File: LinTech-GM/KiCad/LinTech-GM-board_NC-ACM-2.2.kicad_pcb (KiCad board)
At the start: 2 copper layers, 168.9 x 106.7 mm, 78 parts, among them Q1 12000 KHz, X1 Conn_01x08_Male, X2 Conn_01x08_Male, X3 Conn_01x08_Male, X4 Conn_01x08_Male, X7 Conn_02x03_Counter_Clockwise

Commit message: Initial 2
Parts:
- R1: value R1 -> 3.3K
- R11: value R11 -> K10
- R12: value R12 -> 3.3K
- R13, R3: value R -> 470
- R14: value R14 -> 47K
- R2, R4: value R -> 1K
- R5: value R5 -> 150
- R6: value R6 -> 91R
- R7: value R7 -> 91R
- R9: value R9 -> 470 ??
- VD1: value VD1 -> КД522Б
- VD2: value VD2 -> КД522Б
- VD3: value VD3 -> КД522Б
- VD4: value ~ -> КД522Б
- VT1, VT4: value КТ315Б -> КТ646Б
- VT5: value КТ315Б -> КТ313Б ?
- moved VD3 12.7 mm to (203.2, 70.5), turned to 0 degrees
- moved VD4 12.7 mm to (205.7, 114.9), turned to 180 degrees
- moved VD1 12.7 mm to (80.0, 36.2), turned to 270 degrees
- moved VD2 12.7 mm to (63.5, 32.4), turned to 0 degrees
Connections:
- DD3 pad 7: Net-(DD3-Pad7) -> DD5-OE
- R9 pad 1: Net-(R9-Pad1) -> Net-(R10-Pad1)
- VD1 pad 1: /DD10_Out11 -> +5V
- VD1 pad 2: +5V -> /DD10_Out11
- VD2 pad 1: Net-(DD10-Pad1) -> +5V
- VD2 pad 2: +5V -> Net-(DD10-Pad1)
- VD3 pad 1: Net-(C3-Pad1) -> +5V
- VD3 pad 2: +5V -> Net-(C3-Pad1)
- VD4 pad 1: +5V -> Net-(R14-Pad2)
- VD4 pad 2: Net-(R14-Pad2) -> +5V
- VT3 pad 2: Net-(VT3-Pad2) -> +5V
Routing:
- net DD5-OE: track 163.7 -> 178.5 mm
- net +5V: track 855.5 -> 860.5 mm
- net Net-(R10-Pad1): track 2.54 -> 5.08 mm
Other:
- board text added: "Reconstruction by Gryphon@Night-Gryphon.ru"

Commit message: BOM
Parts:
- C12: value C12 -> ~
- C3: value C3 -> ~
- DD5: value Conn_02x12_Counter_Clockwise -> Socket DIP24
- NR1: value R_Network09 -> 3.3K ?
- NR2: value R_Network09 -> ~
- R10: value R10 -> ~
- R9: value 470 ?? -> 470
- SAjp1, SAjp2, SAjp4, SAjp5, SAjp7, SAjp8: value Jumper_NO_Small -> ~
- SAjp3, SAjp6: value Jumper_NC_Small -> ~
- VT5: value КТ313Б ? -> КТ313Б
- X1, X2, X3, X4: value Conn_01x08_Male -> ~
- XA.1, XA.2: value Conn_01x31_Male -> ~

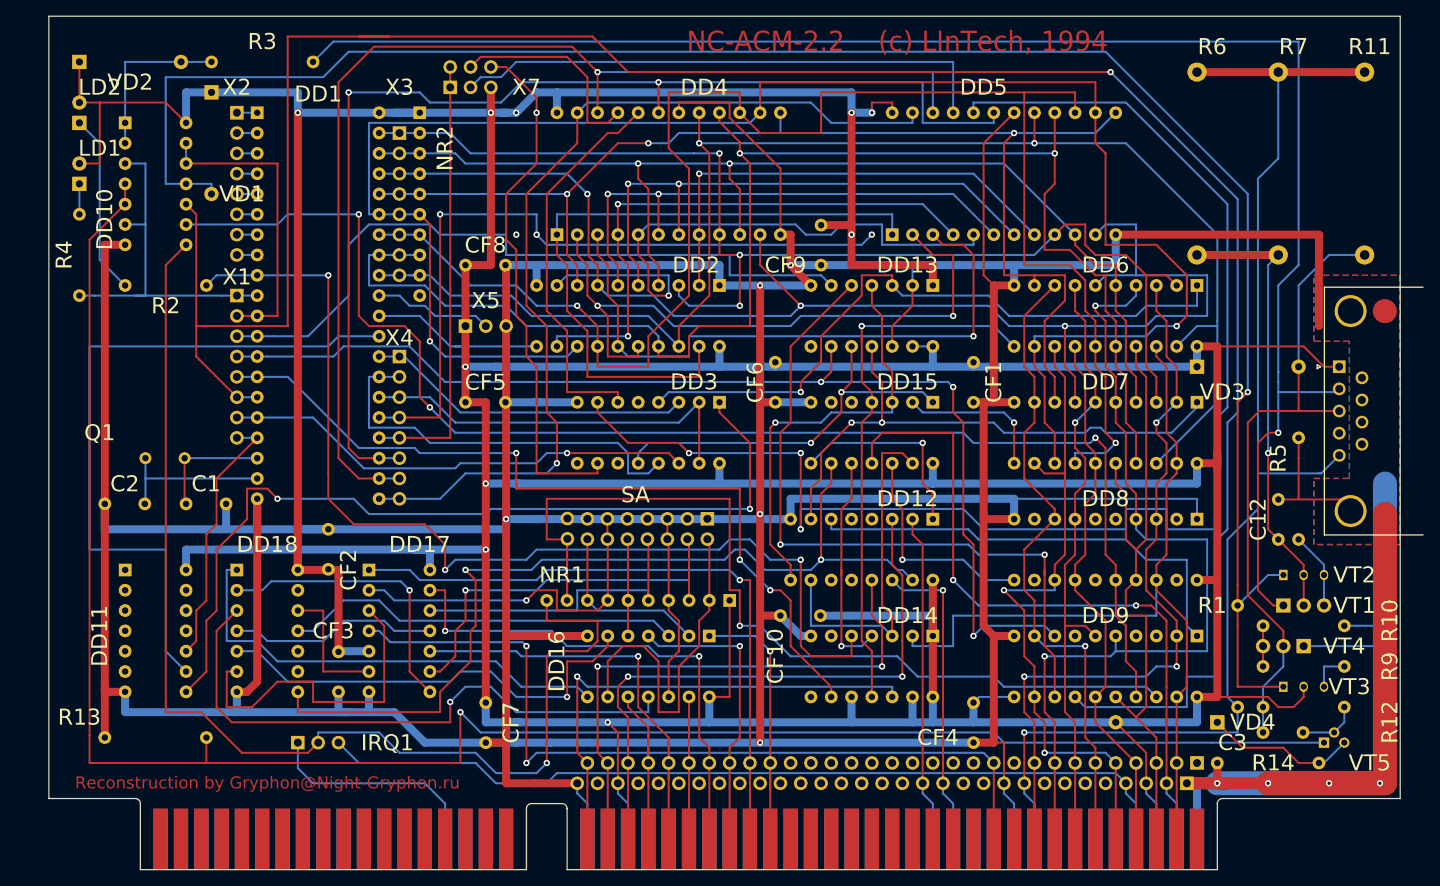
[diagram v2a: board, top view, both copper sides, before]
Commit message: Update GM schematic, README, split LInTech software archive
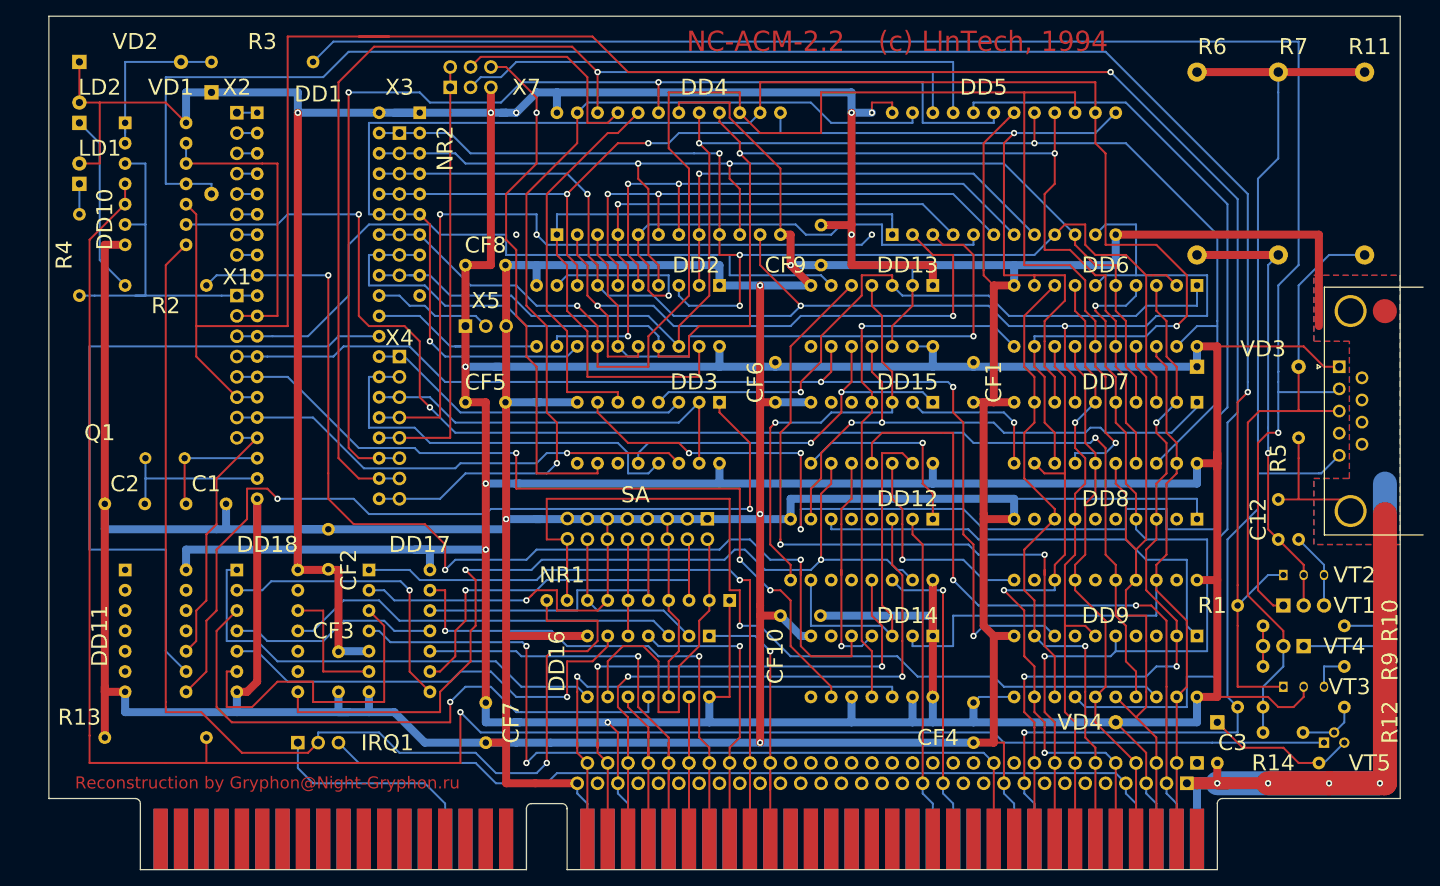
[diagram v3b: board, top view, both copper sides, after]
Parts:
- C1, C2: value C -> 18pF
- C12: value ~ -> 0.15 мкФ
- C3: value ~ -> 1нФ ?
- CF1, CF10, CF2, CF3, CF4, CF5, CF6, CF7, CF8, CF9: value C -> 150nF
- LD1: value LD1 -> LED Red 4mm
- LD2: value LD2 -> LED Red 4mm
- R10: value ~ -> 150
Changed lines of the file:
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@@
       (effects (font (size 2 2) (thickness 0.3)))
     )
-    (fp_text value LD1 (at 1.27 3.46 90) (layer F.Fab)
+    (fp_text value "LED Red 4mm" (at 1.27 3.46 90) (layer F.Fab)
       (effects (font (size 1 1) (thickness 0.15)))
     )
@@
       (effects (font (size 2 2) (thickness 0.3)))
     )
-    (fp_text value LD2 (at 1.27 3.46 90) (layer F.Fab) hide
+    (fp_text value "LED Red 4mm" (at 1.27 3.46 90) (layer F.Fab) hide
       (effects (font (size 1 1) (thickness 0.15)))
     )
@@
       (effects (font (size 2 2) (thickness 0.3)))
     )
-    (fp_text value ~ (at 5.08 2.37) (layer F.Fab)
+    (fp_text value 150 (at 5.08 2.37) (layer F.Fab)
       (effects (font (size 1 1) (thickness 0.15)))
     )
@@
     (descr "Diode, A-405 series, Axial, Horizontal, pin pitch=12.7mm, , length*diameter=5.2*2.7mm^2, , http://www.diodes.com/_files/packages/A-405.pdf")
     (tags "Diode A-405 series Axial Horizontal pin pitch 12.7mm  length 5.2mm diameter 2.7mm")
-    (fp_text reference VD1 (at 12.7 -3.81 180) (layer F.SilkS)
+    (fp_text reference VD1 (at -0.635 5.08) (layer F.SilkS)
       (effects (font (size 2 2) (thickness 0.3)))
     )
@@
     (descr "Diode, A-405 series, Axial, Horizontal, pin pitch=12.7mm, , length*diameter=5.2*2.7mm^2, , http://www.diodes.com/_files/packages/A-405.pdf")
     (tags "Diode A-405 series Axial Horizontal pin pitch 12.7mm  length 5.2mm diameter 2.7mm")
-    (fp_text reference VD3 (at 3.175 3.175) (layer F.SilkS)
+    (fp_text reference VD3 (at 8.255 -2.2225) (layer F.SilkS)
       (effects (font (size 2 2) (thickness 0.3)))
     )
@@
     (descr "Diode, A-405 series, Axial, Horizontal, pin pitch=12.7mm, , length*diameter=5.2*2.7mm^2, , http://www.diodes.com/_files/packages/A-405.pdf")
     (tags "Diode A-405 series Axial Horizontal pin pitch 12.7mm  length 5.2mm diameter 2.7mm")
-    (fp_text reference VD2 (at 6.35 2.54) (layer F.SilkS)
+    (fp_text reference VD2 (at 6.985 -2.54) (layer F.SilkS)
       (effects (font (size 2 2) (thickness 0.3)))
     )
@@
     (descr "Diode, A-405 series, Axial, Horizontal, pin pitch=12.7mm, , length*diameter=5.2*2.7mm^2, , http://www.diodes.com/_files/packages/A-405.pdf")
     (tags "Diode A-405 series Axial Horizontal pin pitch 12.7mm  length 5.2mm diameter 2.7mm")
-    (fp_text reference VD4 (at -4.445 0) (layer F.SilkS)
+    (fp_text reference VD4 (at 17.145 0) (layer F.SilkS)
       (effects (font (size 2 2) (thickness 0.3)))
     )
@@
       (effects (font (size 2 2) (thickness 0.3)))
     )
-    (fp_text value C (at 2.5 2.5) (layer F.Fab) hide
+    (fp_text value 18pF (at 2.5 2.5) (layer F.Fab) hide
       (effects (font (size 1 1) (thickness 0.15)))
     )
@@
       (effects (font (size 2 2) (thickness 0.3)))
     )
-    (fp_text value ~ (at 2.5 2.5 90) (layer F.Fab)
+    (fp_text value "0.15 мкФ" (at 2.5 2.5 90) (layer F.Fab)
       (effects (font (size 1 1) (thickness 0.15)))
     )
@@
       (effects (font (size 2 2) (thickness 0.3)))
     )
-    (fp_text value ~ (at 2.5 2.5) (layer F.Fab) hide
+    (fp_text value "1нФ ?" (at 2.5 2.5) (layer F.Fab) hide
       (effects (font (size 1 1) (thickness 0.15)))
     )
@@
       (effects (font (size 2 2) (thickness 0.3)))
     )
-    (fp_text value C (at 2.5 2.5) (layer F.Fab) hide
+    (fp_text value 18pF (at 2.5 2.5) (layer F.Fab) hide
       (effects (font (size 1 1) (thickness 0.15)))
     )
@@
       (effects (font (size 2 2) (thickness 0.3)))
     )
-    (fp_text value C (at 2.5 2.5) (layer F.Fab) hide
+    (fp_text value 150nF (at 2.5 2.5) (layer F.Fab) hide
       (effects (font (size 1 1) (thickness 0.15)))
     )
@@
       (effects (font (size 2 2) (thickness 0.3)))
     )
-    (fp_text value C (at 2.5 2.5 90) (layer F.Fab) hide
+    (fp_text value 150nF (at 2.5 2.5 90) (layer F.Fab) hide
       (effects (font (size 1 1) (thickness 0.15)))
     )
@@
       (effects (font (size 2 2) (thickness 0.3)))
     )
-    (fp_text value C (at 2.5 2.5) (layer F.Fab) hide
+    (fp_text value 150nF (at 2.5 2.5) (layer F.Fab) hide
       (effects (font (size 1 1) (thickness 0.15)))
     )
@@
       (effects (font (size 2 2) (thickness 0.3)))
     )
-    (fp_text value C (at 2.5 2.5 90) (layer F.Fab) hide
+    (fp_text value 150nF (at 2.5 2.5 90) (layer F.Fab) hide
       (effects (font (size 1 1) (thickness 0.15)))
     )
@@
       (effects (font (size 2 2) (thickness 0.3)))
     )
-    (fp_text value C (at 2.5 2.5 90) (layer F.Fab) hide
+    (fp_text value 150nF (at 2.5 2.5 90) (layer F.Fab) hide
       (effects (font (size 1 1) (thickness 0.15)))
     )
@@
       (effects (font (size 2 2) (thickness 0.3)))
     )
-    (fp_text value C (at 2.5 2.5) (layer F.Fab) hide
+    (fp_text value 150nF (at 2.5 2.5) (layer F.Fab) hide
       (effects (font (size 1 1) (thickness 0.15)))
     )
@@
       (effects (font (size 2 2) (thickness 0.3)))
     )
-    (fp_text value C (at 2.5 2.5 90) (layer F.Fab) hide
+    (fp_text value 150nF (at 2.5 2.5 90) (layer F.Fab) hide
       (effects (font (size 1 1) (thickness 0.15)))
     )
@@
       (effects (font (size 2 2) (thickness 0.3)))
     )
-    (fp_text value C (at 2.5 2.5 90) (layer F.Fab) hide
+    (fp_text value 150nF (at 2.5 2.5 90) (layer F.Fab) hide
       (effects (font (size 1 1) (thickness 0.15)))
     )
@@
       (effects (font (size 2 2) (thickness 0.3)))
     )
-    (fp_text value C (at 2.5 2.5 90) (layer F.Fab) hide
+    (fp_text value 150nF (at 2.5 2.5 90) (layer F.Fab) hide
       (effects (font (size 1 1) (thickness 0.15)))
     )
@@
       (effects (font (size 2 2) (thickness 0.3)))
     )
-    (fp_text value C (at 2.5 2.5 90) (layer F.Fab) hide
-      (effects (font (size 1 1) (thickness 0.15)))
-    )
+    (fp_text value 150nF (at 2.5 2.5 90) (layer F.Fab) hide
+      (effects (font (size 1 1) (thickness 0.15)))
+    )

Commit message: Update GM board silkscreen and 3D render
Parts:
- renumbered IRQ1 to IRQ

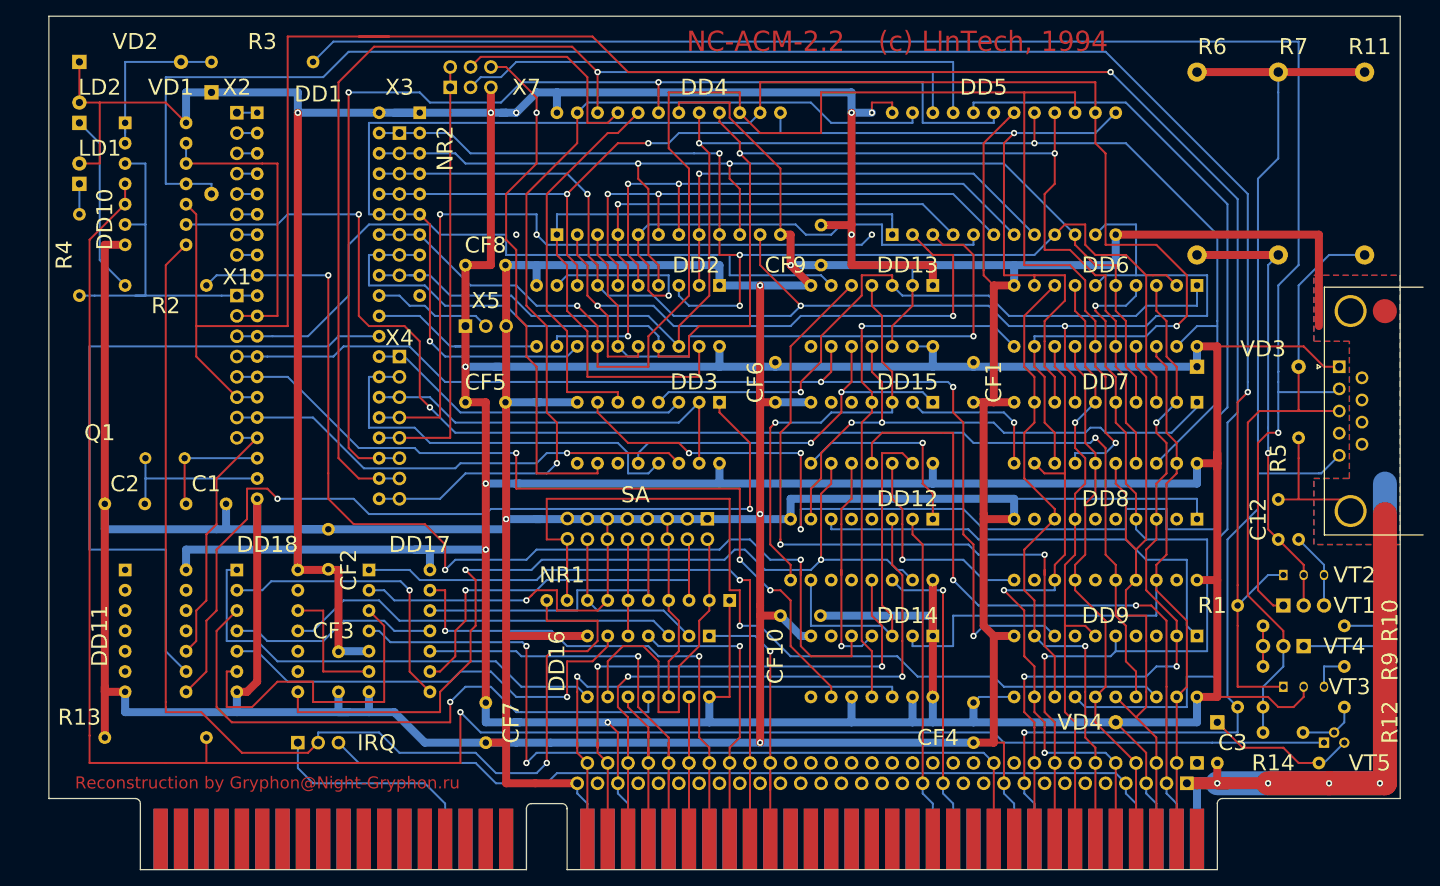
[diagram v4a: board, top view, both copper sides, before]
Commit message: Fix footprint drill diameters
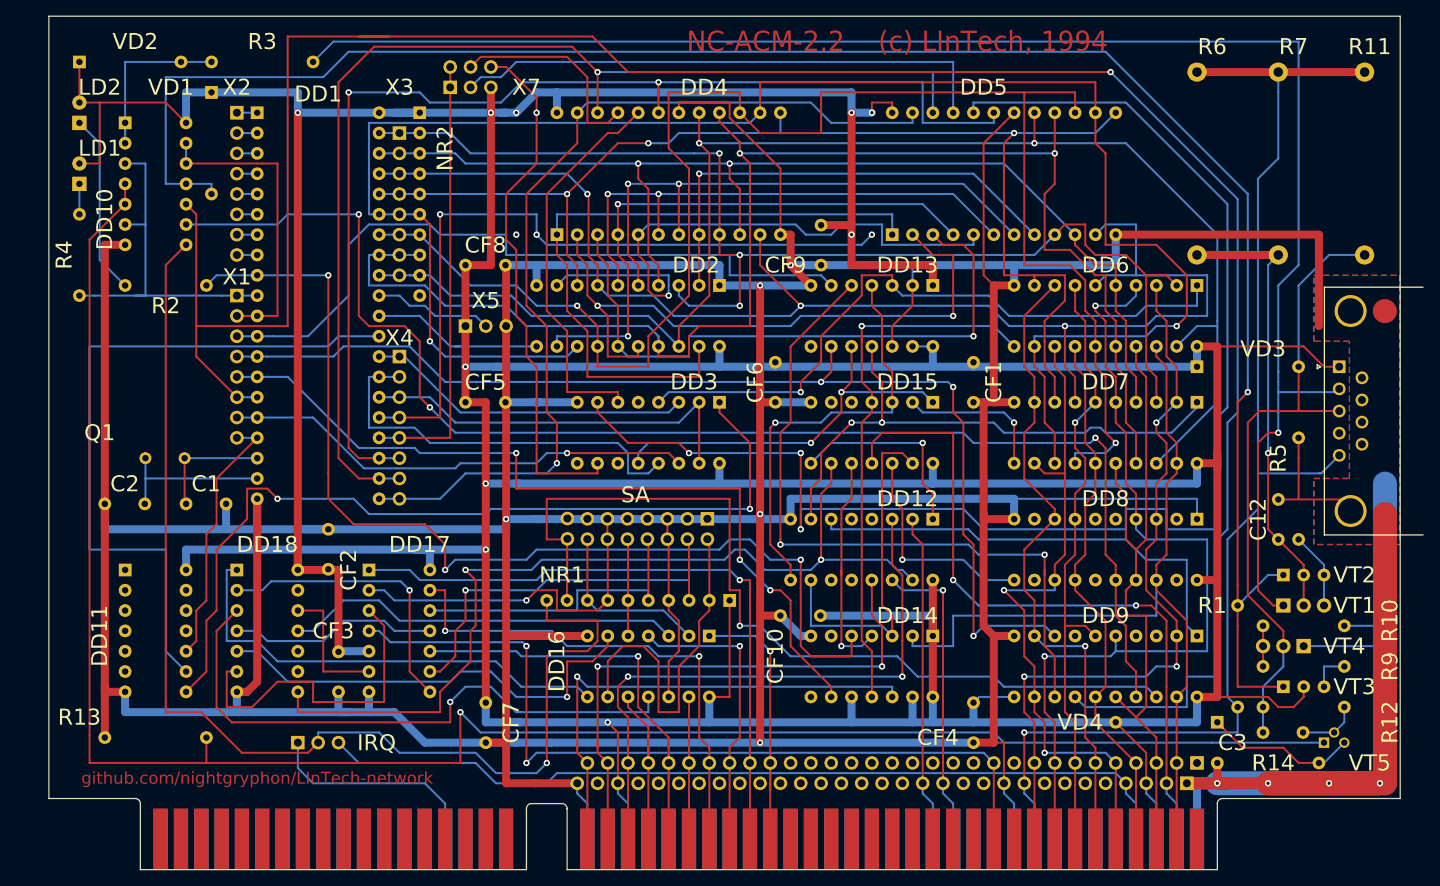
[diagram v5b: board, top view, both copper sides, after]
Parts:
- LD1, LD2: footprint LED_THT:LED_D4.0mm -> lib:LED_D4.0mm
- VT2, VT3: footprint Package_TO_SOT_THT:TO-92S_Wide -> lib:TO-92S_Wide
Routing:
- net +5V: vias 11 -> 10
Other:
- board text added: "github.com/nightgryphon/LInTech-network"
- board text removed: "Reconstruction by Gryphon@Night-Gryphon.ru"

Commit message: Adjust test pads, track width, DB9
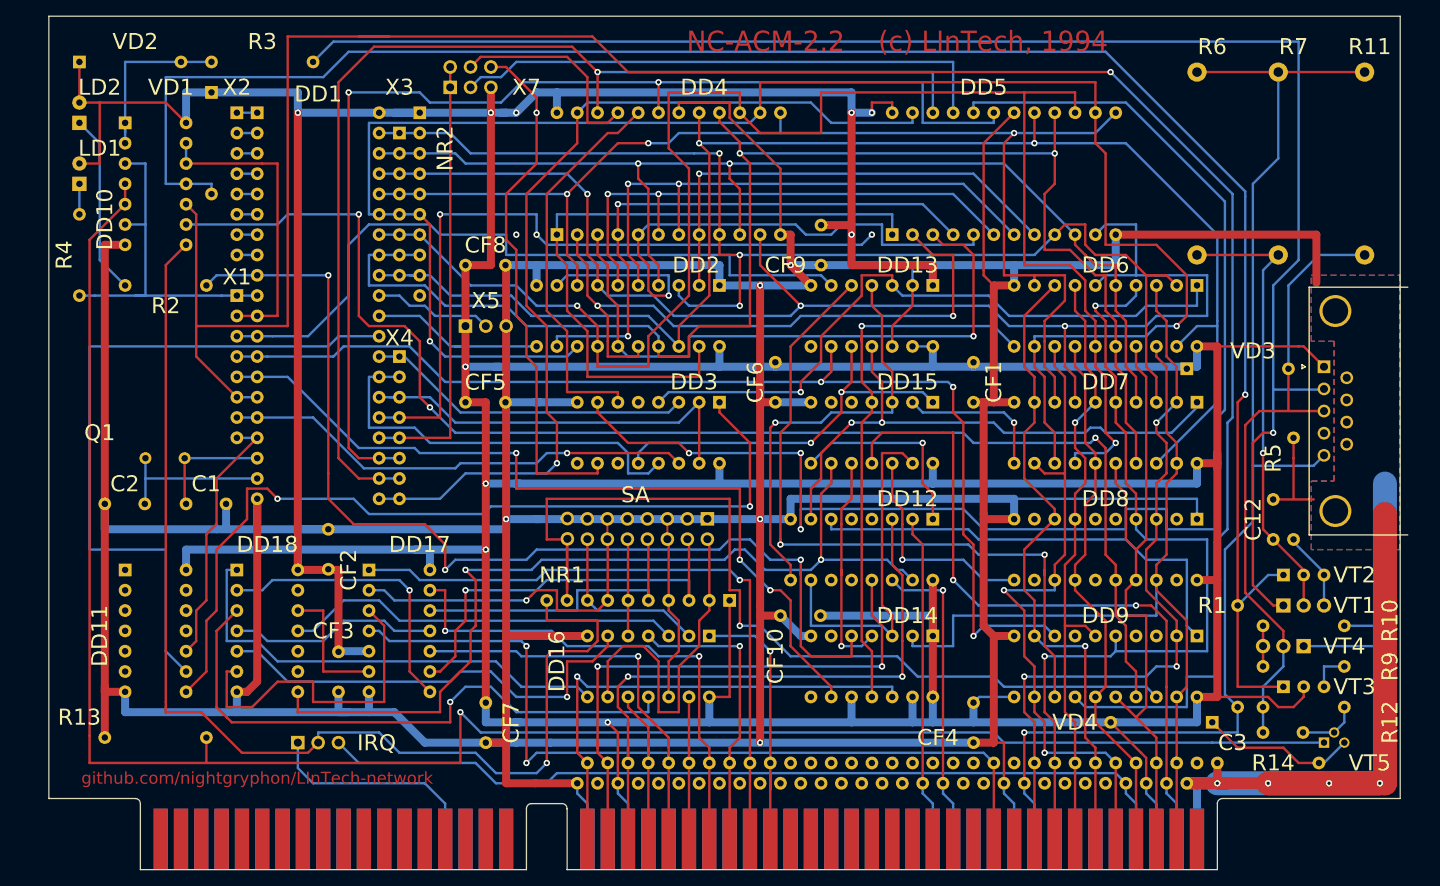
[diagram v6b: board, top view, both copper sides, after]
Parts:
- XA.1, XA.2: footprint Connector_PinHeader_2.54mm:PinHeader_1x31_P2.54mm_Vertical -> lib:PinHeader_1x31_P2.54mm_Vertical
- moved XL1 1.91 mm to (219.1, 70.5)
- moved VD3 1.30 mm to (201.9, 70.7)
- moved C12 0.64 mm to (212.7, 92.1)
- moved R5 0.64 mm to (215.3, 92.1)
- moved VD4 0.64 mm to (205.1, 114.9)
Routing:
- net GND: track 999.7 -> 985.7 mm
- net +5V: track 860.5 -> 858.6 mm
- net +12V: track 158.3 -> 156.9 mm
- net MCU_P3-5: track 291.4 -> 290.0 mm
- net Net-(R3-Pad1): track 207.5 -> 206.6 mm
- net Net-(C12-Pad1): track 56.3 -> 57.2 mm
- net Net-(C3-Pad1): track 80.0 -> 79.1 mm
- net Net-(R14-Pad2): track 18.4 -> 19.0 mm
- net /PROM_RD: track 107.9 -> 107.4 mm
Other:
- net class Default: trace_width 0.25 -> 0.3
